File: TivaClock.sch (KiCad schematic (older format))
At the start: 6 parts, among them J1 Conn_01x10, J2 Conn_01x10, J3 Conn_01x10, J4 Conn_01x10, J5 Conn_01x20, J6 Conn_01x20

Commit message: added footprints and locations
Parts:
- J1, J2, J3, J4: footprint (none) -> Pin_Headers:Pin_Header_Straight_1x10_Pitch2.54mm
- J5, J6: footprint (none) -> Pin_Headers:Pin_Header_Straight_1x20_Pitch2.54mm
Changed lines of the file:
@@
 F 0 "J1" H 2800 2800 50  0000 C CNN
 F 1 "Conn_01x10" H 2800 1700 50  0000 C CNN
-F 2 "" H 2800 2300 50  0001 C CNN
+F 2 "Pin_Headers:Pin_Header_Straight_1x10_Pitch2.54mm" H 2800 2300 50  0001 C CNN
 F 3 "" H 2800 2300 50  0001 C CNN
 	1    2800 2300
@@
 F 0 "J3" H 3350 2800 50  0000 C CNN
 F 1 "Conn_01x10" H 3350 1700 50  0000 C CNN
-F 2 "" H 3350 2300 50  0001 C CNN
+F 2 "Pin_Headers:Pin_Header_Straight_1x10_Pitch2.54mm" H 3350 2300 50  0001 C CNN
 F 3 "" H 3350 2300 50  0001 C CNN
 	1    3350 2300
@@
 F 0 "J4" H 7800 2800 50  0000 C CNN
 F 1 "Conn_01x10" H 7800 1700 50  0000 C CNN
-F 2 "" H 7800 2300 50  0001 C CNN
+F 2 "Pin_Headers:Pin_Header_Straight_1x10_Pitch2.54mm" H 7800 2300 50  0001 C CNN
 F 3 "" H 7800 2300 50  0001 C CNN
 	1    7800 2300
@@
 F 0 "J2" H 8500 2800 50  0000 C CNN
 F 1 "Conn_01x10" H 8500 1700 50  0000 C CNN
-F 2 "" H 8500 2300 50  0001 C CNN
+F 2 "Pin_Headers:Pin_Header_Straight_1x10_Pitch2.54mm" H 8500 2300 50  0001 C CNN
 F 3 "" H 8500 2300 50  0001 C CNN
 	1    8500 2300
@@
 F 0 "J5" H 5200 5550 50  0000 C CNN
 F 1 "Conn_01x20" H 5200 3450 50  0000 C CNN
-F 2 "" H 5200 4550 50  0001 C CNN
+F 2 "Pin_Headers:Pin_Header_Straight_1x20_Pitch2.54mm" H 5200 4550 50  0001 C CNN
 F 3 "" H 5200 4550 50  0001 C CNN
 	1    5200 4550
@@
 F 0 "J6" H 5950 5650 50  0000 C CNN
 F 1 "Conn_01x20" H 5950 3550 50  0000 C CNN
-F 2 "" H 5950 4650 50  0001 C CNN
+F 2 "Pin_Headers:Pin_Header_Straight_1x20_Pitch2.54mm" H 5950 4650 50  0001 C CNN
 F 3 "" H 5950 4650 50  0001 C CNN
 	1    5950 4650

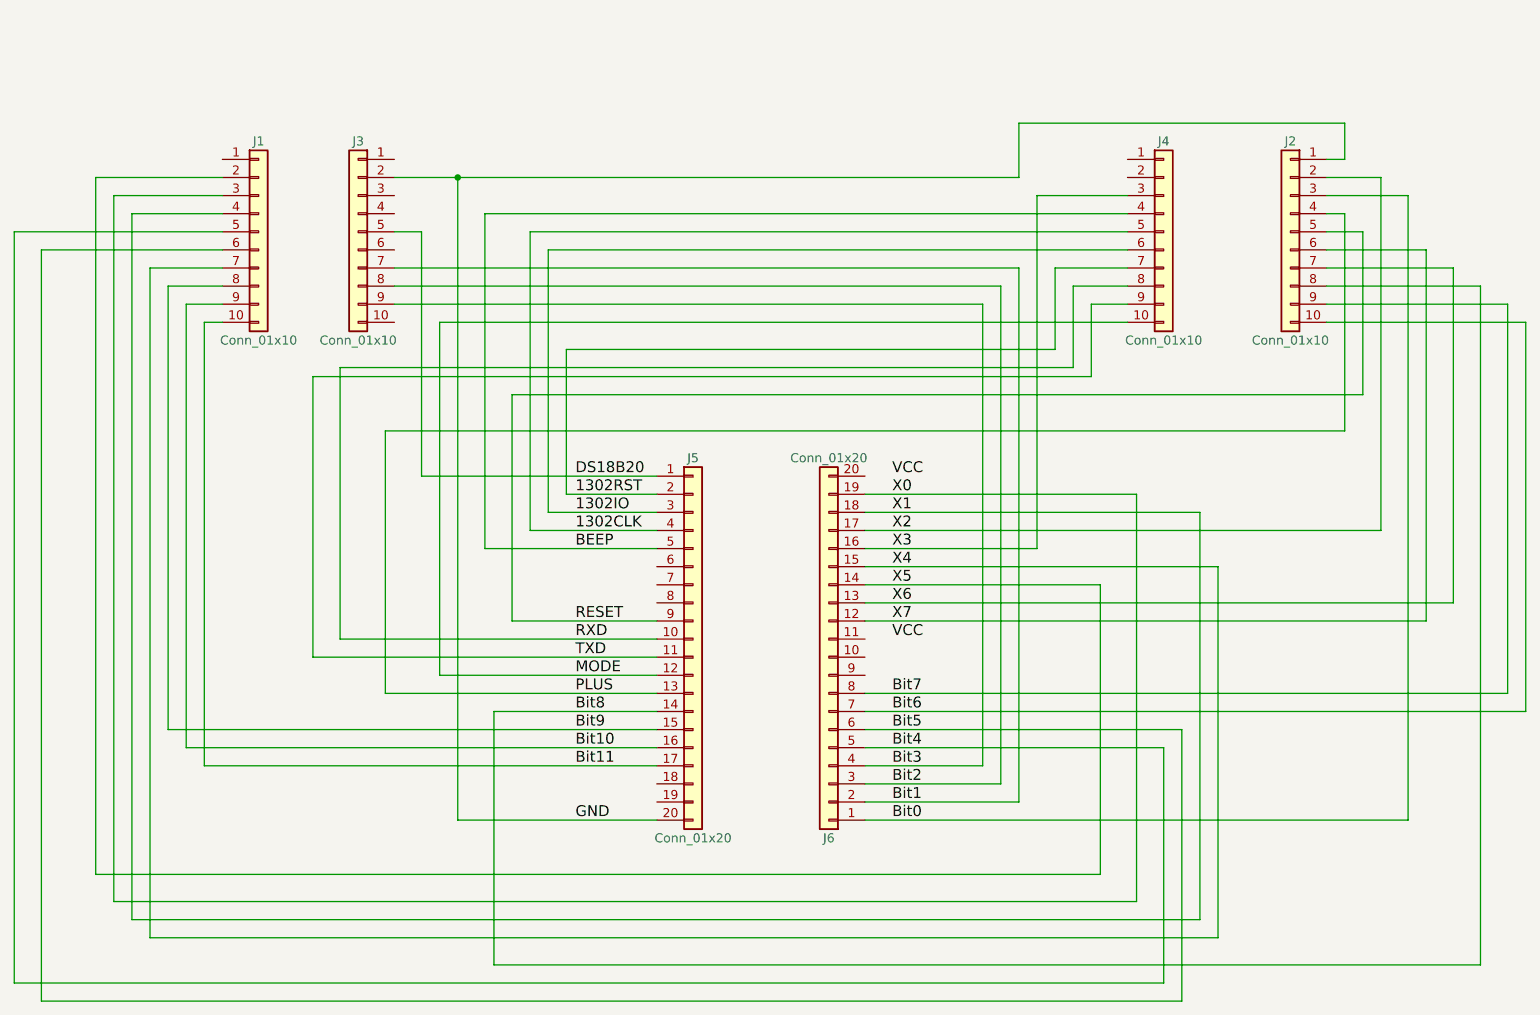
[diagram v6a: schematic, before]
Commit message: add jumper to connect 3.3V or 5V to board VCC
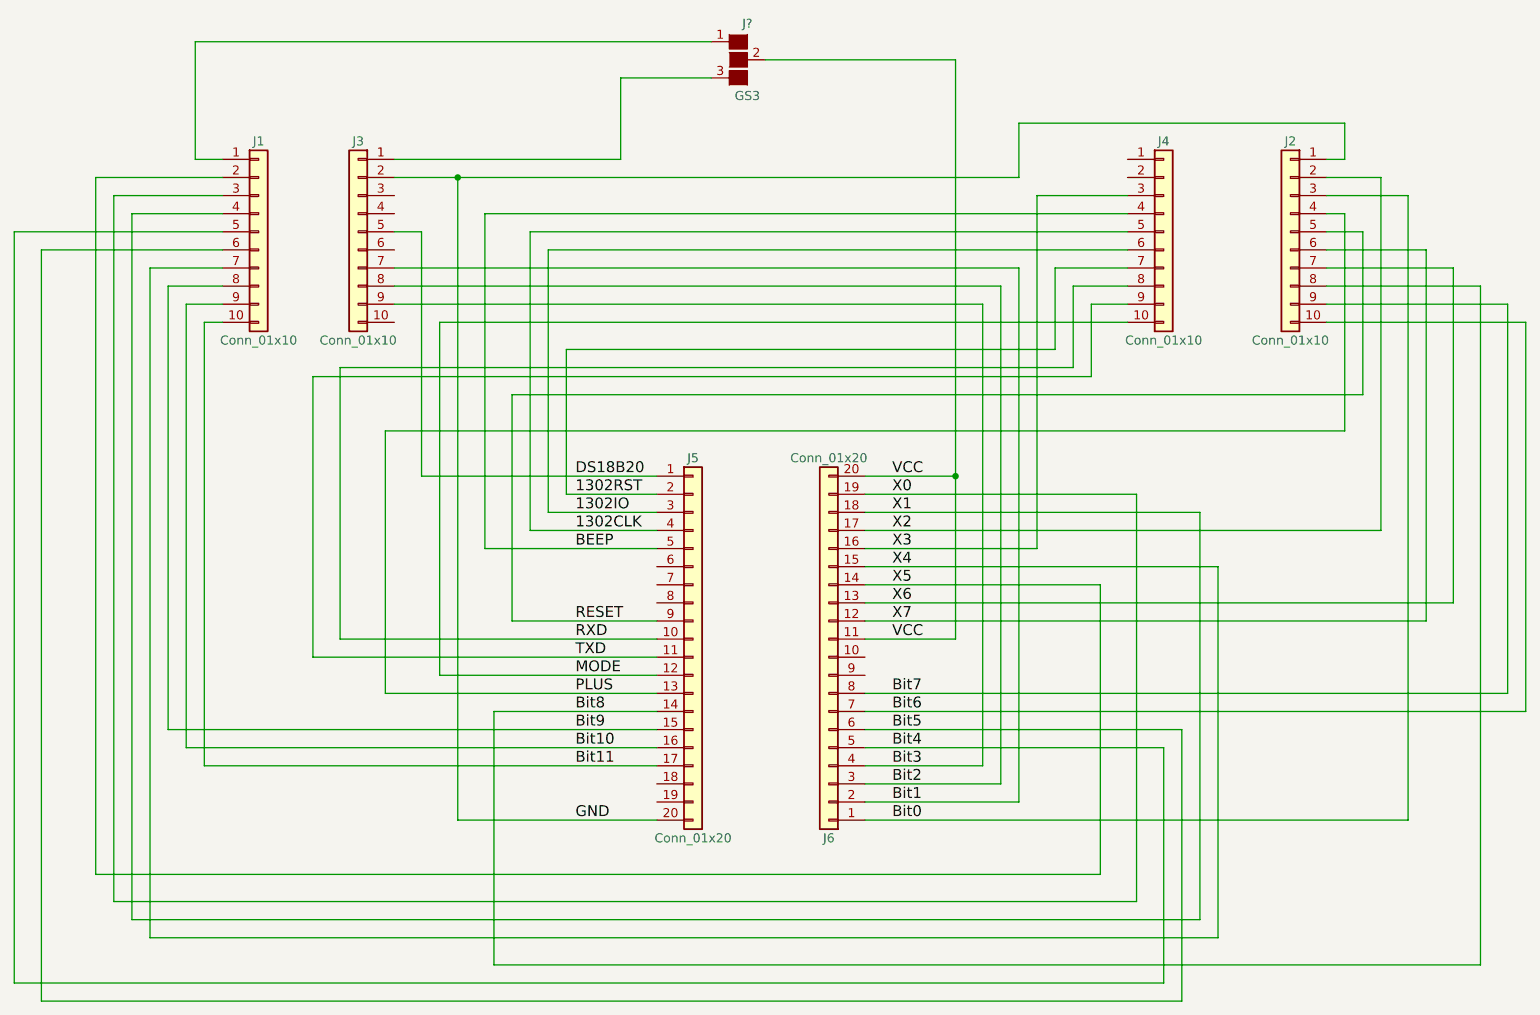
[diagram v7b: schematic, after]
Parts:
- added J?: GS3, Connectors:GS3, symbol GS3
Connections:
- net VCC: now also J6.11 (Pin_11), J6.20 (Pin_20), J?.2 (G2)
- net at J1.1 (Pin_1): now also J?.1 (G1)
- net at J3.1 (Pin_1): now also J?.3 (G3)
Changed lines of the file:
@@
 Wire Wire Line
 	3100 4650 5000 4650
+$Comp
+L GS3 J?
+U 1 1 5A6B36DA
+P 5450 1350
+F 0 "J?" H 5500 1550 50  0000 C CNN
+F 1 "GS3" H 5500 1151 50  0000 C CNN
+F 2 "Connectors:GS3" V 5538 1276 50  0001 C CNN
+F 3 "" H 5450 1350 50  0001 C CNN
+	1    5450 1350
+	1    0    0    -1
+$EndComp
+Wire Wire Line
+	5600 1350 6650 1350
+Wire Wire Line
+	6650 1350 6650 4550
+Wire Wire Line
+	6650 3650 6150 3650
+Wire Wire Line
+	6650 4550 6150 4550
+Connection ~ 6650 3650
+Wire Wire Line
+	5300 1250 2450 1250
+Wire Wire Line
+	2450 1250 2450 1900
+Wire Wire Line
+	2450 1900 2600 1900
+Wire Wire Line
+	3550 1900 4800 1900
+Wire Wire Line
+	4800 1900 4800 1450
+Wire Wire Line
+	4800 1450 5300 1450
 $EndSCHEMATC

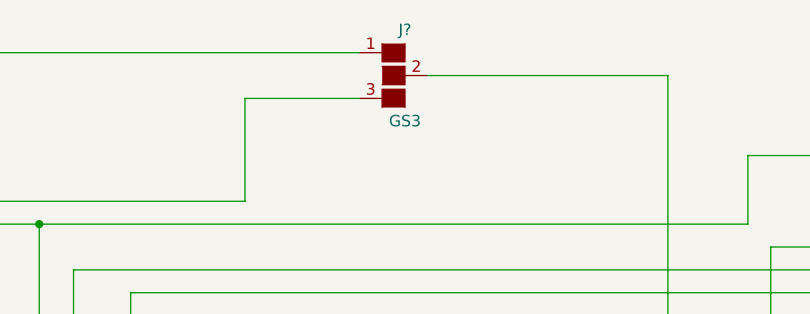
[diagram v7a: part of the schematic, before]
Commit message: put solder jumper on PCB
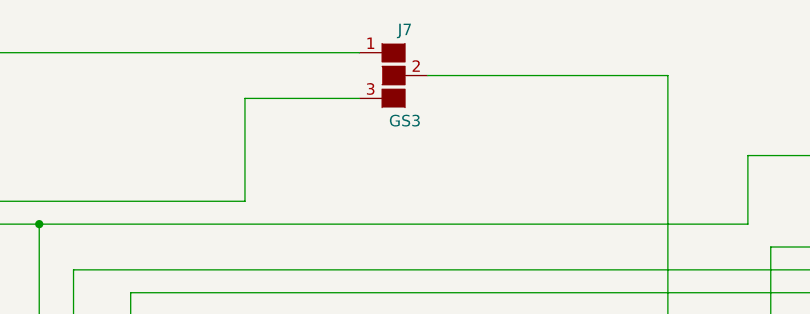
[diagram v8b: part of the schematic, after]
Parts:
- gave numbers to parts that had none: 1
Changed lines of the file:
@@
 	3100 4650 5000 4650
 $Comp
-L GS3 J?
+L GS3 J7
 U 1 1 5A6B36DA
 P 5450 1350
-F 0 "J?" H 5500 1550 50  0000 C CNN
+F 0 "J7" H 5500 1550 50  0000 C CNN
 F 1 "GS3" H 5500 1151 50  0000 C CNN
 F 2 "Connectors:GS3" V 5538 1276 50  0001 C CNN
